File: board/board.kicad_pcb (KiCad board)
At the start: 4 copper layers, 21 x 77 mm, 66 parts, among them J1 UART, J2 008_USB, J3 DebugEdge_02x05, J4 019_100BASE-T_with_CT, J5 ADC_2x3, J7 SPI_2x3, J8 I2C_2x2, J9 UART_2x2, U1 W25Q128JVS, U2 RP2040, U3 W5500, U4 11AA02E48, Y1 12MhZ, Y2 25MHz

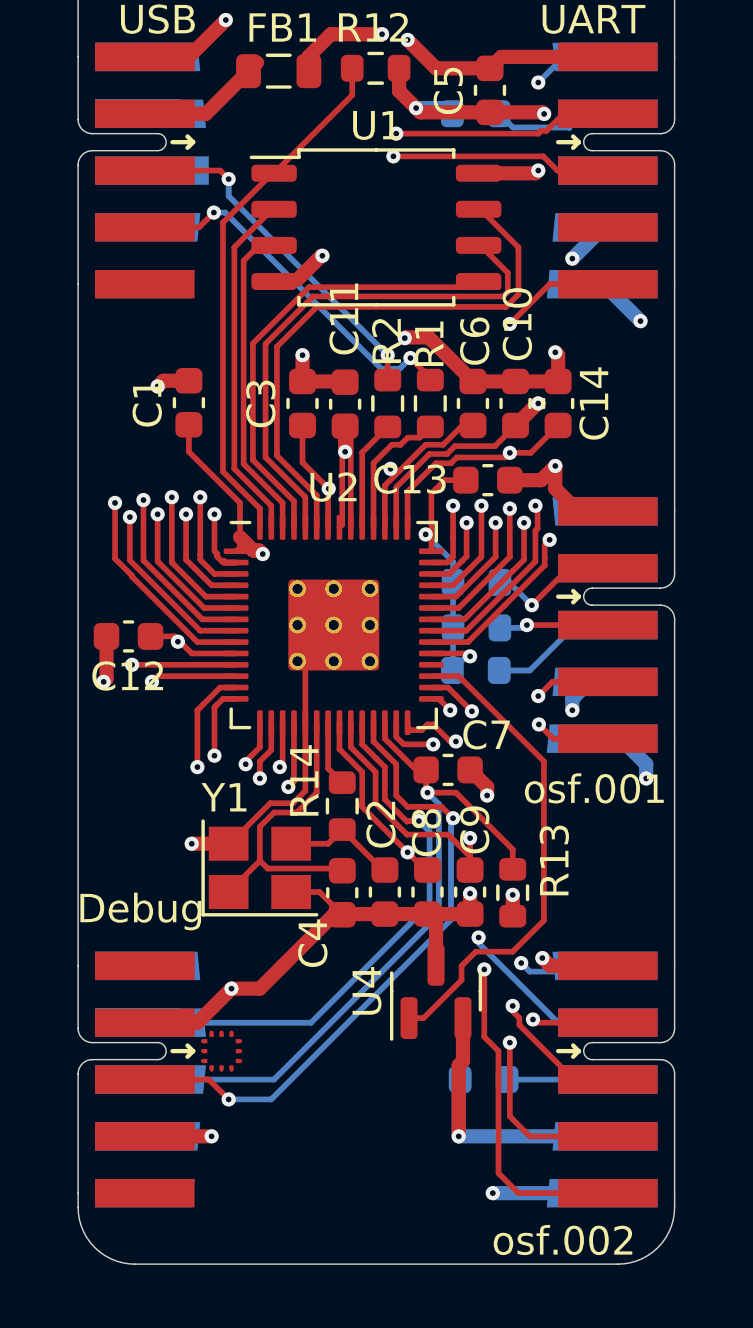
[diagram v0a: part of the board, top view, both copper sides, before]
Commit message: added needle addapter
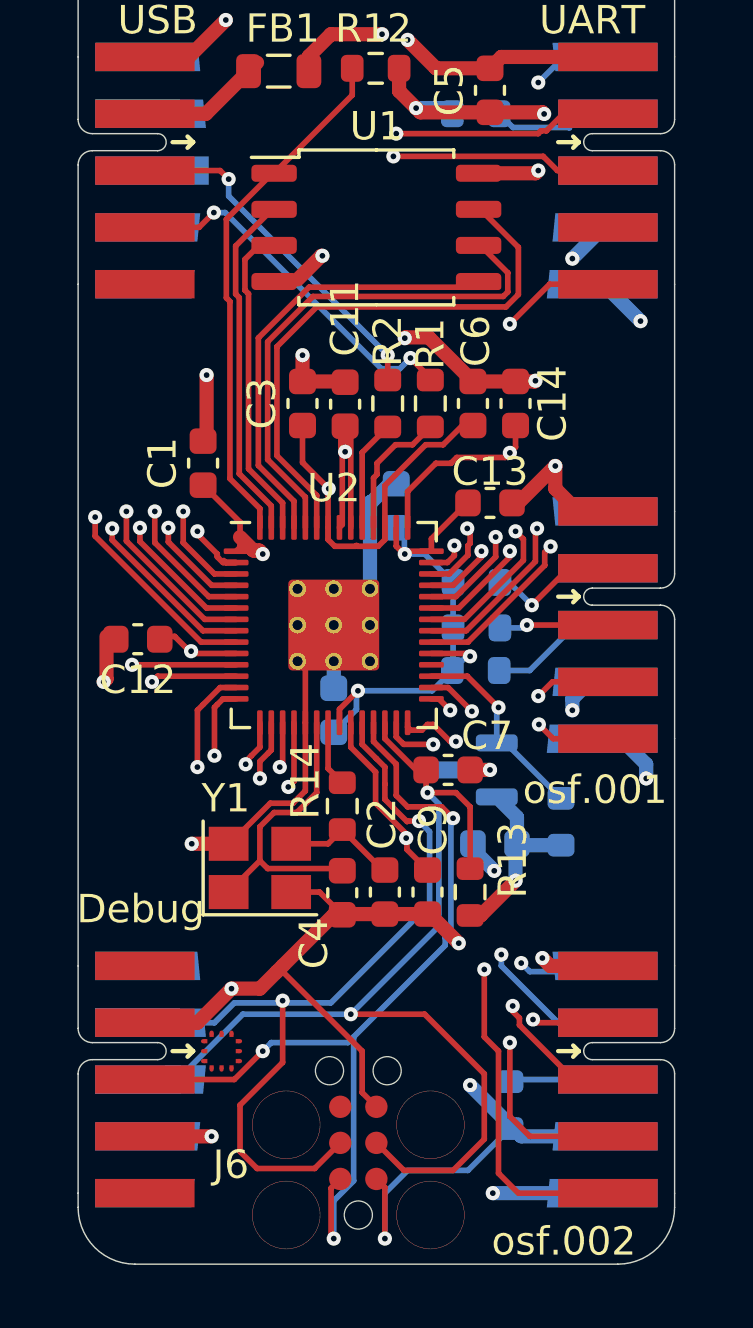
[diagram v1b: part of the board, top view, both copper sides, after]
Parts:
- added C28: 100nF, Capacitor_SMD:C_0603_1608Metric, B.Cu at (154.7, 88.2)
- added J6: SWD_6_Pol_Needle, c001:SWD6pol, F.Cu at (150.5, 100.0)
- added R24: 2k, Resistor_SMD:R_0603_1608Metric, B.Cu at (157.0, 87.4)
- C10, C8, U4: moved to B.Cu
- C7: value 1nF -> 1uF
- moved U4 7.89 mm to (153.8, 85.6), turned to 180 degrees
- moved C8 7.20 mm to (149.0, 83.5), turned to 90 degrees
- moved C10 5.53 mm to (151.2, 76.3)
- moved C1 2.18 mm to (144.4, 74.8)
- moved R13 1.50 mm to (153.8, 89.9)
- moved C14 1.50 mm to (155.4, 72.7)
- moved C9 1.50 mm to (152.3, 89.9)
- moved R9 1.29 mm to (155.2, 97.4), turned to 90 degrees
- moved C13 0.80 mm to (154.5, 76.2)
- moved C12 0.34 mm to (142.1, 81.0)
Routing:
- net /rp2040/RUN: track 25.1 -> 37.2 mm, vias 1 -> 2
- net GND: track 263.6 -> 274.6 mm, vias 25 -> 26
- net /mac/IO: track 17.3 -> 7.16 mm, vias 0 -> 1
- net /rp2040/SWCLK: track 19.6 -> 29.7 mm, vias 1 -> 2
- net /rp2040/SWD: track 22.5 -> 32.0 mm, vias 2 -> 3
- net +3V3: track 194.2 -> 189.4 mm
- net Net-(C3-Pad1): track 36.6 -> 32.4 mm, vias 3 -> 2
- net /GPIO24: track 41.9 -> 44.0 mm
- net Net-(C14-Pad1): track 37.4 -> 36.3 mm
- net /UART0_RX: track 42.2 -> 42.7 mm
- net /GPIO25: track 51.6 -> 51.0 mm
- net /rp2040/SPI0_SCK: track 47.9 -> 48.5 mm
- net /rp2040/GPIO7: track 58.0 -> 58.5 mm

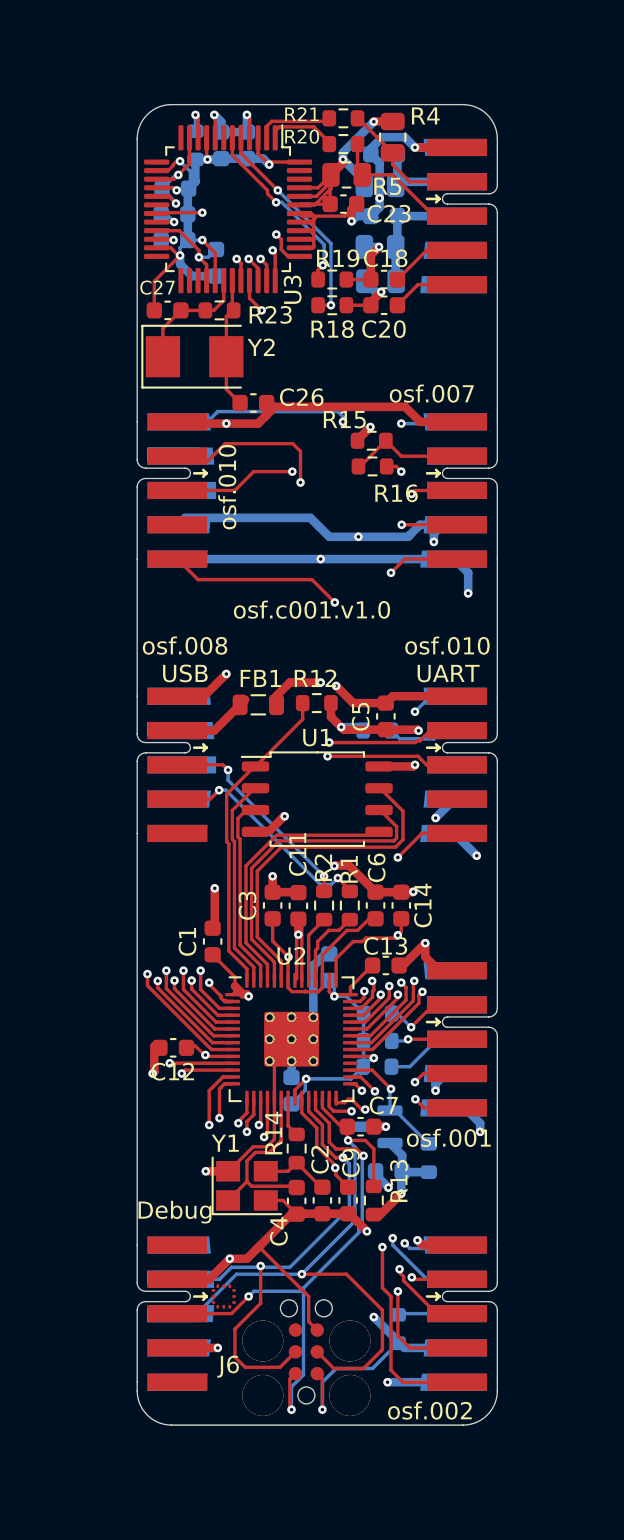
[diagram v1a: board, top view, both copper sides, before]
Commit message: added power planes
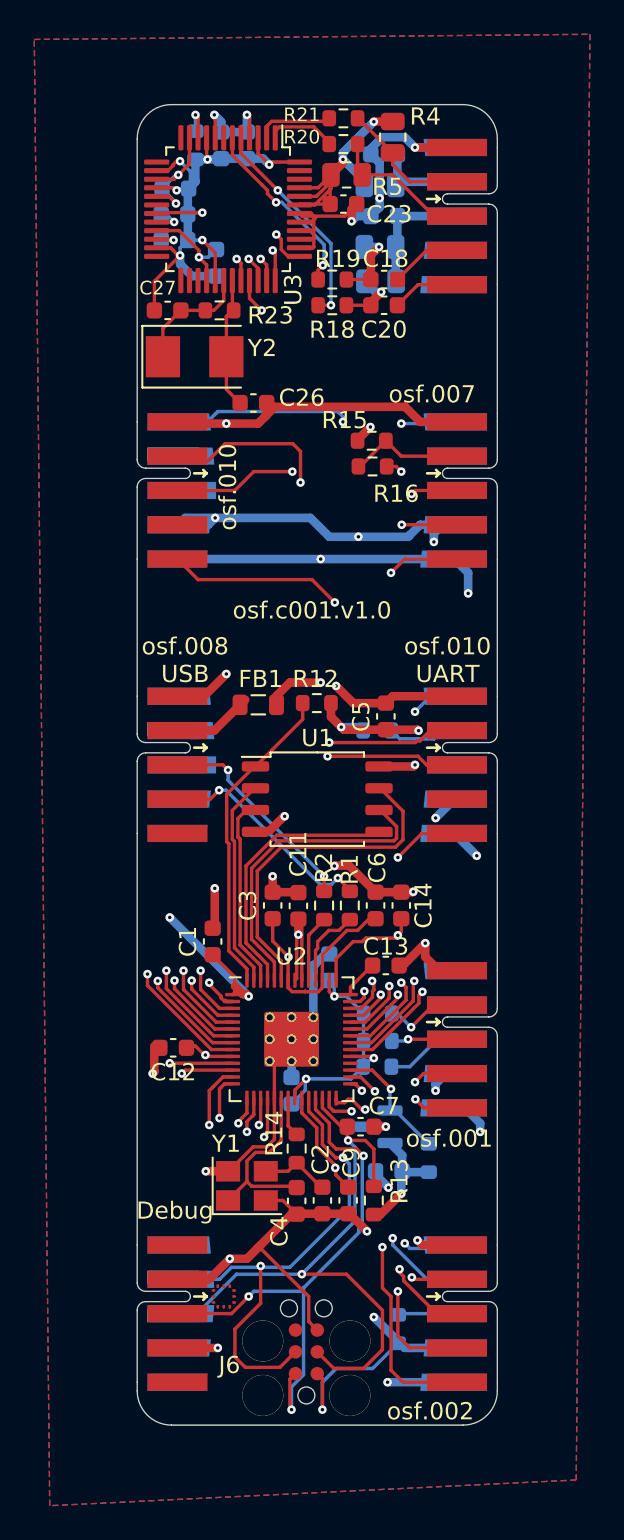
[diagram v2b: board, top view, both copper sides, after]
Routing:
- net +3V3: track 189.4 -> 198.2 mm, vias 18 -> 20
- added copper zone on In1.Cu, net +3V3
- added copper zone on B.Cu, net GND
- added copper zone on F.Cu, net GND
- added copper zone on In2.Cu, net GND
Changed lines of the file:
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@@
   (via (at 156.2 64.5) (size 0.5) (drill 0.2) (layers "F.Cu" "B.Cu") (net 1))
   (via (at 157.4 83.5) (size 0.5) (drill 0.2) (layers "F.Cu" "B.Cu") (net 1))
+  (via (at 144.5465 50.1) (size 0.5) (drill 0.2) (layers "F.Cu" "B.Cu") (net 1))
   (via (at 156.406644 62.506644) (size 0.5) (drill 0.2) (layers "F.Cu" "B.Cu") (net 1))
   (via (at 155.4 89.5) (size 0.5) (drill 0.2) (layers "F.Cu" "B.Cu") (net 1))
+  (via (at 141.9 73.4) (size 0.5) (drill 0.2) (layers "F.Cu" "B.Cu") (net 1))
   (via (at 151.9 62.3) (size 0.5) (drill 0.2) (layers "F.Cu" "B.Cu") (net 1))
   (via (at 153.8 81.6) (size 0.5) (drill 0.2) (layers "F.Cu" "B.Cu") (net 1))
@@
   (segment (start 150.1 50.1) (end 142.8 50.1) (width 0.5) (layer "B.Cu") (net 1))
   (segment (start 151.5 78) (end 151.499294 78) (width 0.2) (layer "B.Cu") (net 1))
+  (segment (start 144.1465 50.5) (end 144.5465 50.1) (width 0.5) (layer "B.Cu") (net 1))
   (segment (start 151.2 51.2) (end 150.6 50.6) (width 0.5) (layer "B.Cu") (net 1))
   (segment (start 155.45 87.2625) (end 154.7375 86.55) (width 0.5) (layer "B.Cu") (net 1))
@@
   (segment (start 151.499294 78) (end 151.487897 78.011397) (width 0.2) (layer "B.Cu") (net 1))
   (segment (start 151.5 78) (end 152.2 78) (width 0.2) (layer "B.Cu") (net 1))
+  (segment (start 142.4 50.5) (end 144.1465 50.5) (width 0.5) (layer "B.Cu") (net 1))
   (segment (start 150.8 102.1) (end 150.8 100.5) (width 0.2) (layer "B.Cu") (net 1))
   (segment (start 153.2 80.6) (end 153.2 82.075) (width 0.2) (layer "B.Cu") (net 1))
   (segment (start 151.9 62.3) (end 152.975 62.3) (width 0.5) (layer "B.Cu") (net 1))
   (segment (start 152.975 62.3) (end 153.175 62.5) (width 0.5) (layer "B.Cu") (net 1))
+  (segment (start 146.5 78) (end 141.9 73.4) (width 0.5) (layer "B.Cu") (net 1))
   (segment (start 149.8515 82.813086) (end 152.461914 82.813086) (width 0.2) (layer "B.Cu") (net 1))
   (segment (start 151.487897 77.362897) (end 151.2 77.075) (width 0.2) (layer "B.Cu") (net 1))
@@
   (segment (start 154.7375 84.65) (end 154.7375 83.4625) (width 0.2) (layer "B.Cu") (net 84))
   (segment (start 155.05 84.65) (end 154.7375 84.65) (width 0.2) (layer "B.Cu") (net 84))
+  (zone (net 2) (net_name "GND") (layers "F.Cu" "In2.Cu" "B.Cu") (hatch edge 0.508)
+    (connect_pads (clearance 0.2))
+    (min_thickness 0.2) (filled_areas_thickness no)
+    (fill yes (thermal_gap 0.508) (thermal_bridge_width 0.508))
+    (polygon
+      (pts
+        (xy 165.6 106.2)
+        (xy 134.9 107.7)
+        (xy 134 22.2)
+        (xy 166.4 21.9)
+      )
+    )
+  )
+  (zone (net 1) (net_name "+3V3") (layer "In1.Cu") (hatch edge 0.508)
+    (connect_pads (clearance 0.2))
+    (min_thickness 0.2) (filled_areas_thickness no)
+    (fill yes (thermal_gap 0.508) (thermal_bridge_width 0.508))
+    (polygon
+      (pts
+        (xy 164.4 24.1)
+        (xy 163.9 104.9)
+        (xy 137.3 106)
+        (xy 135.7 24)
+      )
+    )
+  )
 )

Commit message: improved power integrity
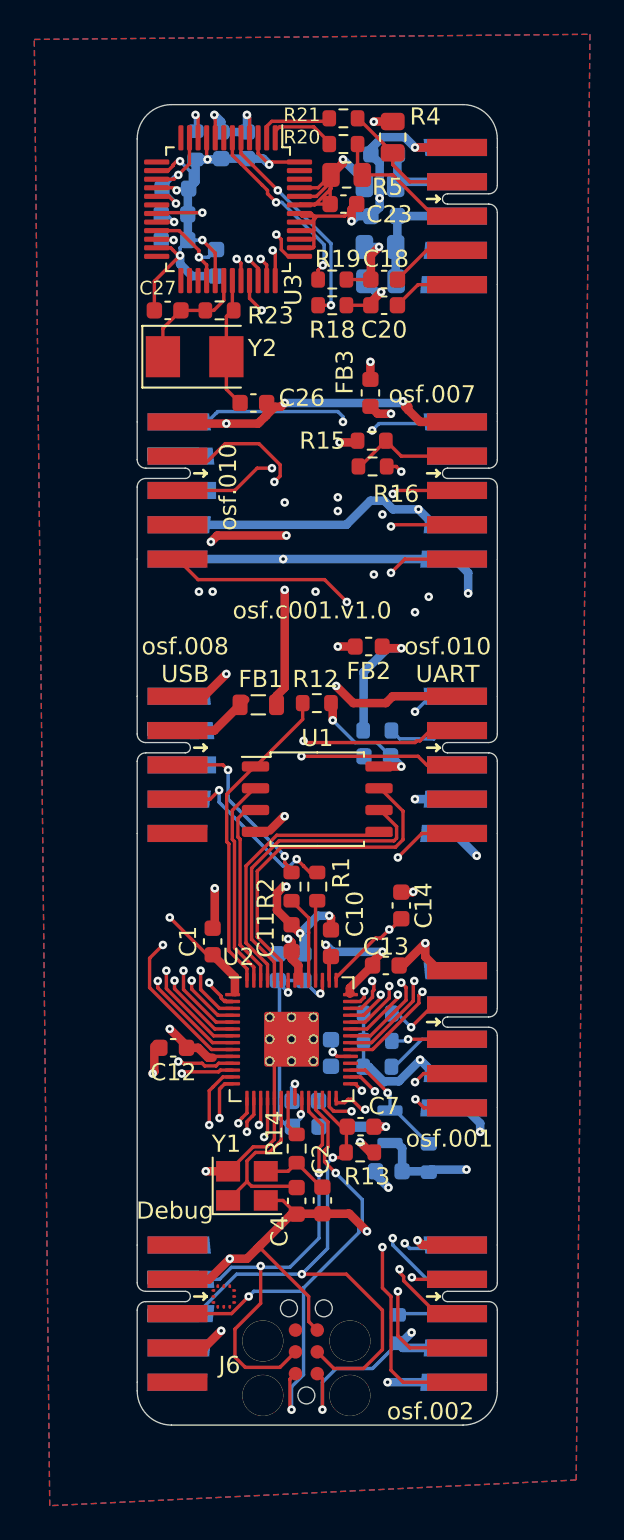
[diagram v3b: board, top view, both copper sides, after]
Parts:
- added C29: 100nF, Capacitor_SMD:C_0603_1608Metric, B.Cu at (151.3, 81.3)
- added FB2: FerriteBead_Small, Inductor_SMD:L_0603_1608Metric, F.Cu at (153.5, 57.6)
- added FB3: FerriteBead_Small, Inductor_SMD:L_0603_1608Metric, F.Cu at (153.6, 42.8)
- C10: moved to F.Cu
- C3, C5, C6, C9: moved to B.Cu
- moved C6 6.74 mm to (148.2, 76.3)
- moved C9 4.96 mm to (149.8, 85.6), turned to 0 degrees
- moved C3 4.02 mm to (149.7, 76.3)
- moved R13 2.91 mm to (153.0, 87.1), turned to 180 degrees
- moved C5 2.38 mm to (154.0, 64.0), turned to 180 degrees
- moved R1 2.20 mm to (150.5, 71.6)
- moved R2 2.20 mm to (149.0, 71.6)
- moved C11 1.92 mm to (149.0, 74.6)
- moved C10 1.40 mm to (151.3, 74.9)
- moved C8 1.00 mm to (149.8, 84.1), turned to 0 degrees
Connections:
- C1 pad 1: +3V3 -> /rp2040/VDD
- C10 pad 1: +3V3 -> /rp2040/VDD
- C11 pad 1: +3V3 -> /rp2040/VDD
- C12 pad 1: +3V3 -> /rp2040/VDD
- C13 pad 1: +3V3 -> /rp2040/VDD
- C5 pad 1: +3V3 -> /rp2040/VDD
- C8 pad 1: +3V3 -> /rp2040/VDD
- R12 pad 1: +3V3 -> /rp2040/VDD
- R13 pad 1: +3V3 -> /rp2040/VDD
- R15 pad 1: +3V3 -> /rp2040/VDD
- U1 pad 8: +3V3 -> /rp2040/VDD
- U2 pad 1: +3V3 -> /rp2040/VDD
- U2 pad 10: +3V3 -> /rp2040/VDD
- U2 pad 22: +3V3 -> /rp2040/VDD
- U2 pad 33: +3V3 -> /rp2040/VDD
- U2 pad 42: +3V3 -> /rp2040/VDD
- U2 pad 44: +3V3 -> /rp2040/VDD
- U2 pad 48: +3V3 -> /rp2040/VDD
- U2 pad 49: +3V3 -> /rp2040/VDD
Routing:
- net /rp2040/VDD: track 0.00 -> 139.5 mm, vias 0 -> 14
- net +3V3: track 198.2 -> 136.2 mm, vias 20 -> 9
- net /controller/VDD: track 61.2 -> 79.2 mm, vias 7 -> 8
- net Net-(C6-Pad1): track 32.4 -> 16.2 mm, vias 2 -> 3
- net GND: track 274.6 -> 284.1 mm, vias 26 -> 39
- net /rp2040/RUN: track 37.2 -> 33.2 mm
- net Net-(U2-Pad43): track 36.3 -> 34.1 mm
- net /UART0_RX: track 42.7 -> 40.5 mm
- net Net-(J2-Pad4): track 13.1 -> 11.1 mm
- net /UART0_TX: track 42.6 -> 40.6 mm
- net +5V: track 90.0 -> 88.1 mm
- net Net-(J2-Pad3): track 12.5 -> 10.6 mm
- net /ADC0: track 36.0 -> 37.6 mm
- net /rp2040/SWCLK: track 29.7 -> 28.2 mm
- net /rp2040/SPI0_SCK: track 48.5 -> 47.1 mm
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- added copper zone on In1.Cu, net /controller/VDD
- added copper zone on In1.Cu, net /rp2040/VDD
- removed copper zone on In1.Cu, net +3V3

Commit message: improved board emc
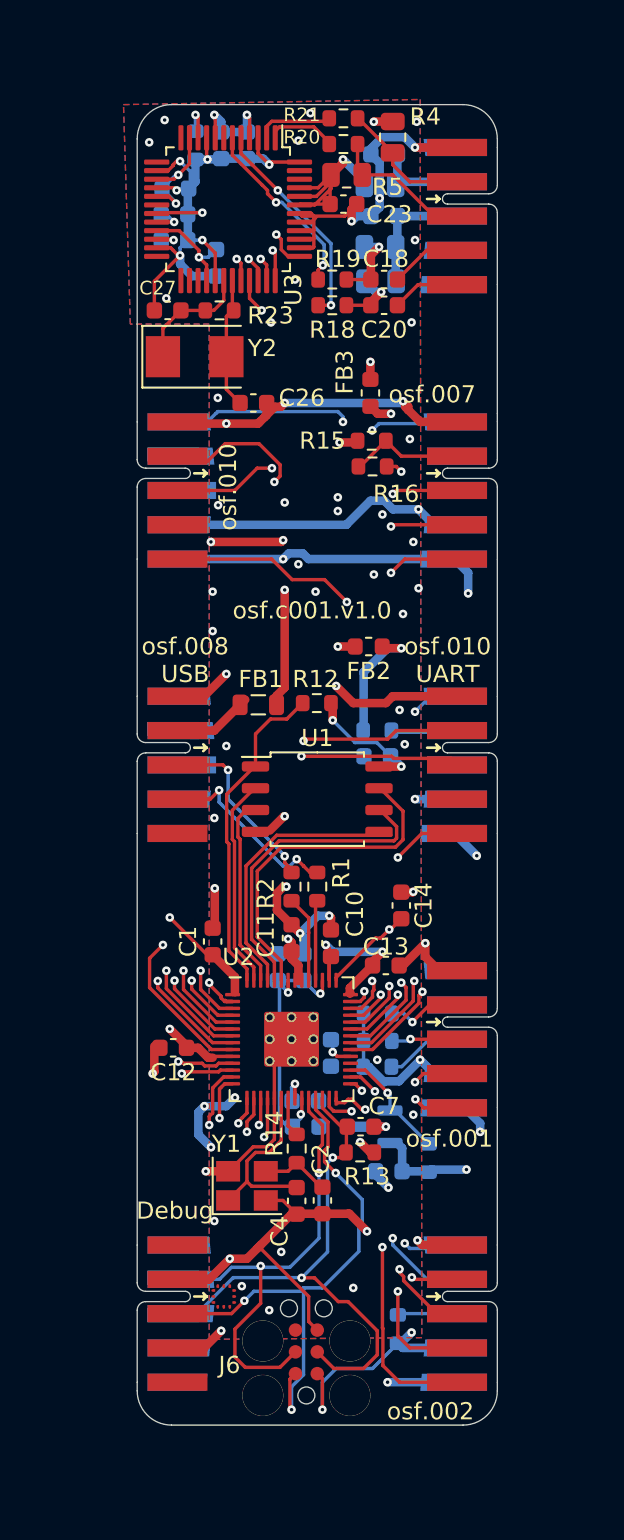
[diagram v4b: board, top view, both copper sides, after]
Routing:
- net GND: track 284.1 -> 288.4 mm, vias 39 -> 68
- net Net-(J9-Pad7): track 2.68 -> 3.91 mm
- net /rp2040/RUN: track 33.2 -> 32.1 mm
- net /rp2040/SWD: track 31.4 -> 32.1 mm
- net /rp2040/QPI_SS: track 18.5 -> 19.1 mm
